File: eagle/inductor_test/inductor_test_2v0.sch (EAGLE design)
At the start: 81 parts, among them J1 MA02-1, U1 OPA2369, U2 OPA2369, U3 SC70, U4 SOT-23-6, U5 TSSOP-14, U6 TPS62122, U7 MAX9910

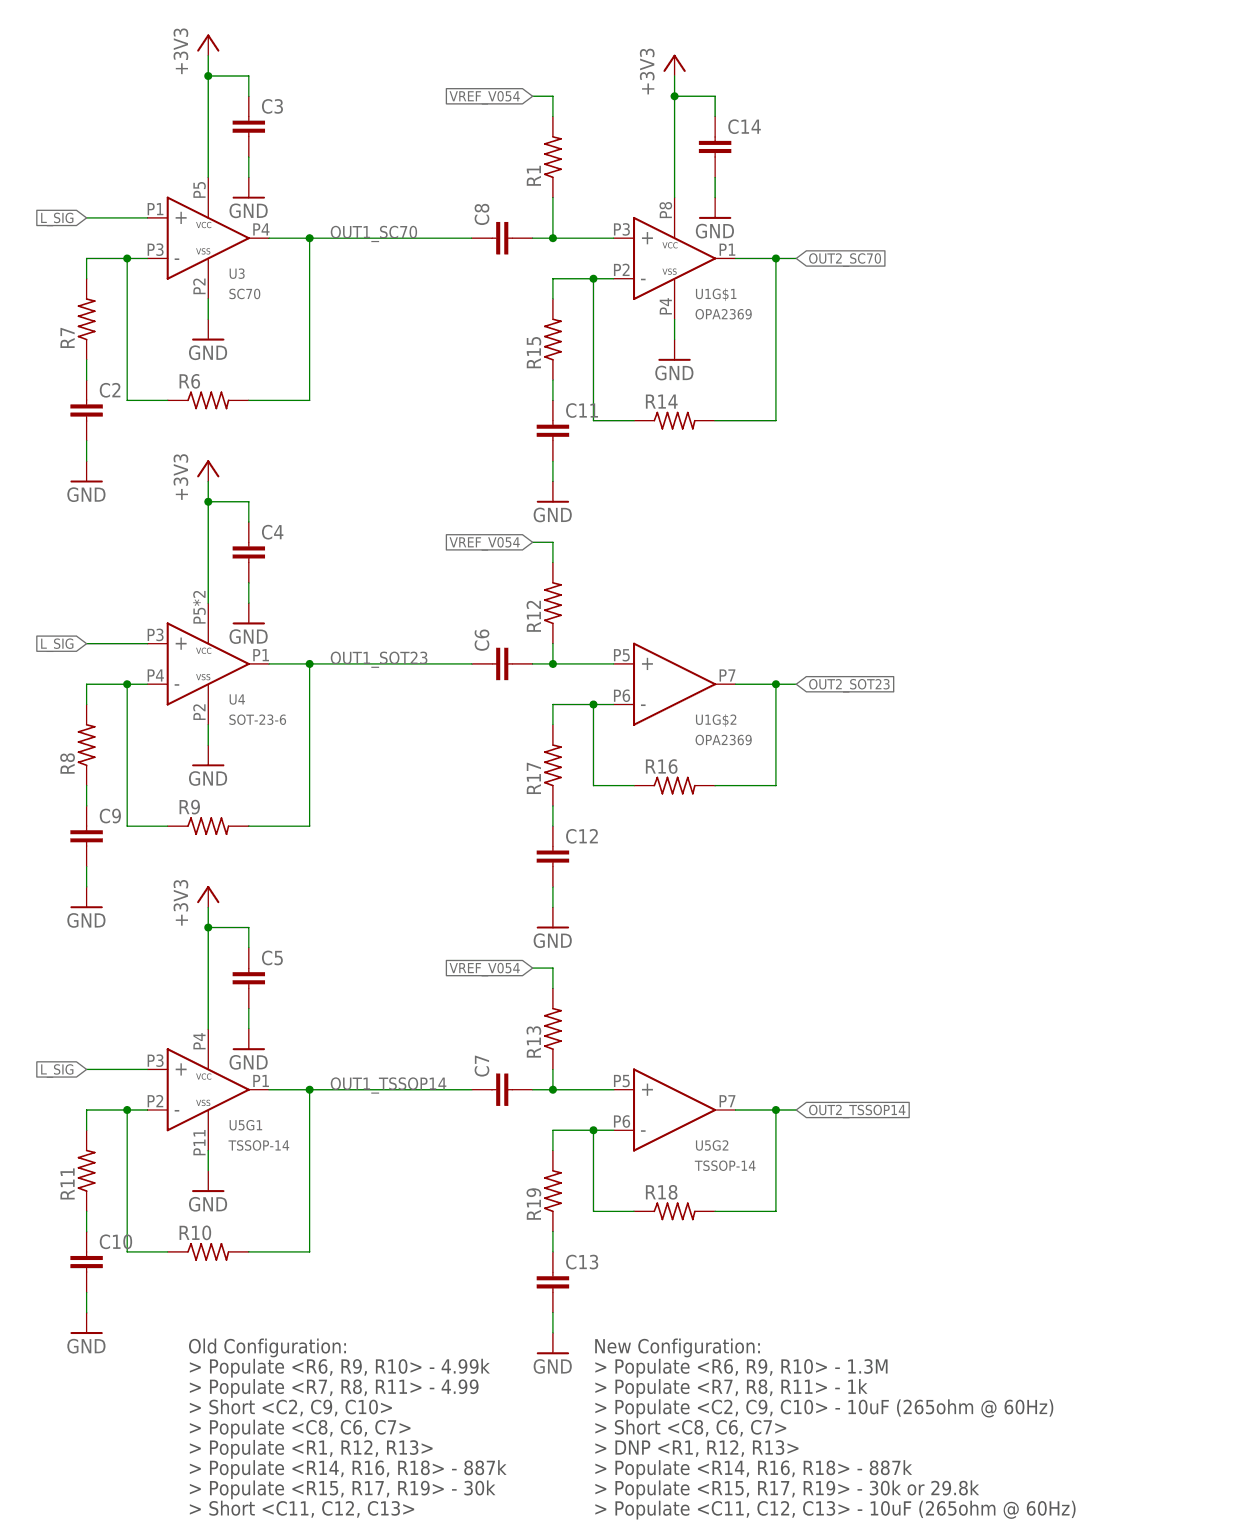
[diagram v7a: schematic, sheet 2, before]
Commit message: added part numbers and values
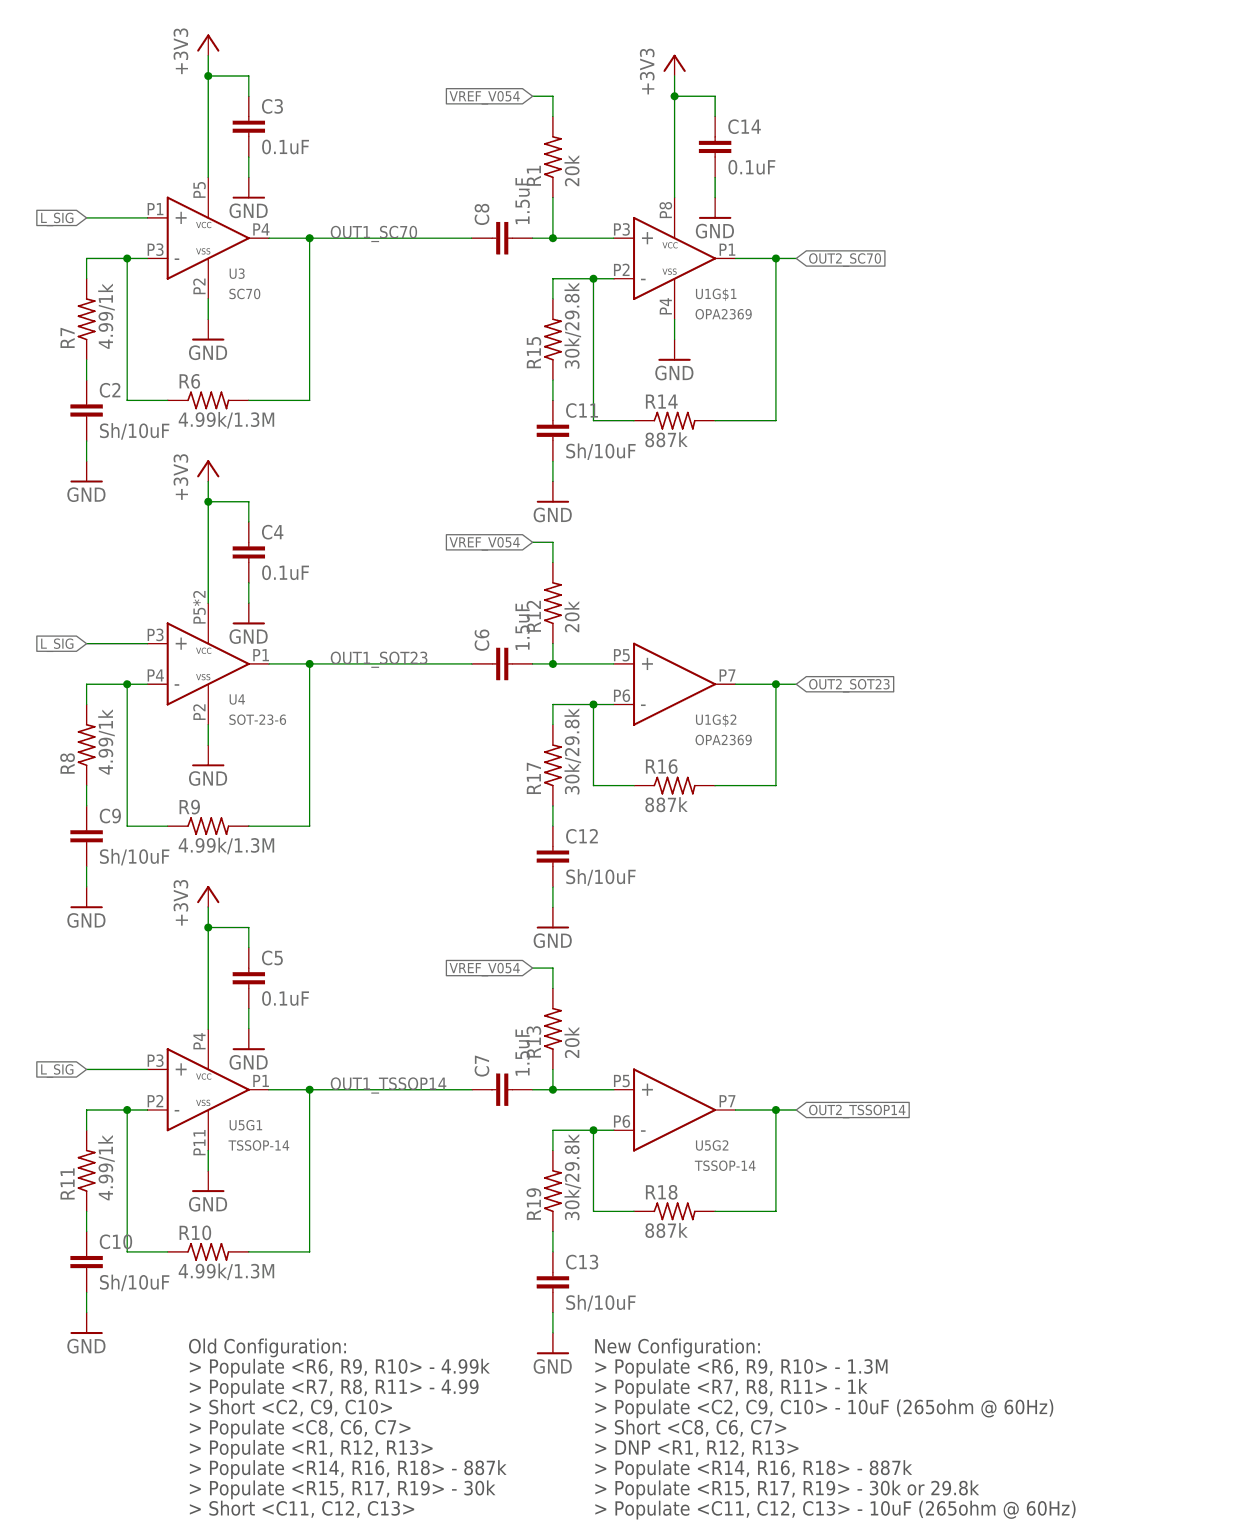
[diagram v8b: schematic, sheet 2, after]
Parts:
- C1, C6, C7, C8: value (none) -> 1.5uF
- C10, C11, C12, C13, C2, C9: value (none) -> Sh/10uF
- C14, C15, C3, C4, C5: value (none) -> 0.1uF
- LED1: DIGIKEY (none) -> 1125-1181-ND
- R1, R12, R13, R5: value (none) -> 20k
- R10, R6, R9: value (none) -> 4.99k/1.3M
- R11, R7, R8: value (none) -> 4.99/1k
- R14, R16, R18: value (none) -> 887k
- R15, R17, R19: value (none) -> 30k/29.8k
- R20, R21, R22: value (none) -> 100k
- R23: value (none) -> 1.6k
- R31: value (none) -> 240
- TP1, TP2: DIGIKEY (none) -> 36-5126-ND
- TP10, TP11, TP12, TP9: DIGIKEY (none) -> 36-5011-ND
- TP3, TP4: DIGIKEY (none) -> 36-5128-ND
- TP5, TP6: DIGIKEY (none) -> 36-5014-ND
- TP7, TP8: DIGIKEY (none) -> 36-5010-ND
